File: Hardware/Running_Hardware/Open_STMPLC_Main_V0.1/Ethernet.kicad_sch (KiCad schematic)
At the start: 19 parts, among them J13 RJ45_Hanrun_HR911105A_Horizon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, U7 LAN8720A, Y3 25MHz

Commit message: PCB routing completion v0.1 Main
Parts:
- added C73: 1nF/2kV, Capacitor_SMD:C_1206_3216Metric_Pad1.33x1.80mm_HandSolder, symbol Device:C_Small
- added R17, R48, R49: 10K, Resistor_SMD:R_0603_1608Metric_Pad0.98x0.95mm_HandSolder, symbol Device:R_Small
- added R30: 1M, Resistor_SMD:R_1206_3216Metric_Pad1.30x1.75mm_HandSolder, symbol Device:R_Small
- U7: footprint Package_DFN_QFN:VQFN-24-1EP_4x4mm_P0.5mm_EP2.5x2.5mm_ThermalVias -> Package_DFN_QFN:VQFN-24-1EP_4x4mm_P0.5mm_EP2.5x2.5mm
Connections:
- net +3V3: no longer R27.2, R28.2
- net GND: now also J13.10, J13.11, C73.2, R17.1, R30.1, R48.2; no longer J13.SH
- net LED1: now also R27.2; no longer J13.11
- net LED2: now also R28.2, R17.2; no longer J13.10
- net at C38.1, C39.1, C40.1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: now also R49.1
- net ETH_RXER renamed PHYAD0
- net PHYAD0: now also R48.1, R49.2
- net Earth: no longer names the net of J13.8
- net Earth: now also J13.SH, C73.1, R30.2
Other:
- moved on the sheet: R27, R28

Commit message: Silkscreen and DRC
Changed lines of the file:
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@@
 	(title_block
 		(title "Open_STMPLC_Main")
-		(date "2026-05-23")
+		(date "2026-05-24")
 		(rev "0.1")
 	)
@@
 		(effects
 			(font
-				(size 1.27 1.27)
+				(size 1 1)
 			)
 			(justify left bottom)
@@
 		(effects
 			(font
-				(size 1.27 1.27)
+				(size 1 1)
 			)
 			(justify left bottom)
@@
 		(effects
 			(font
-				(size 1.27 1.27)
+				(size 1 1)
 			)
 			(justify left bottom)
@@
 		(effects
 			(font
-				(size 1.27 1.27)
+				(size 1 1)
 			)
 			(justify left bottom)
@@
 		(effects
 			(font
-				(size 1.27 1.27)
+				(size 1 1)
 			)
 			(justify left bottom)
@@
 			(effects
 				(font
-					(size 1.27 1.27)
+					(size 1 1)
 				)
 			)
@@
 			(effects
 				(font
-					(size 1.27 1.27)
-				)
-			)
+					(size 1 1)
+				)
+			)

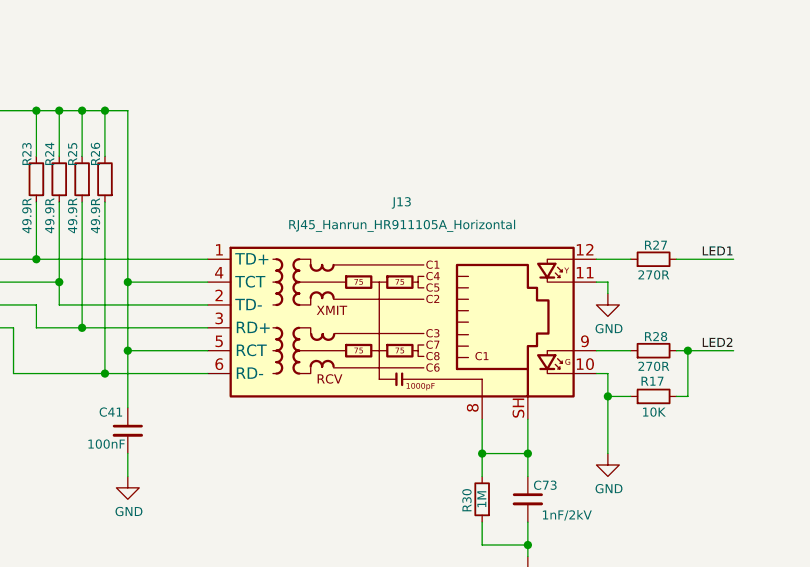
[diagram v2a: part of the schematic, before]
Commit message: Ethernet updated to vertical
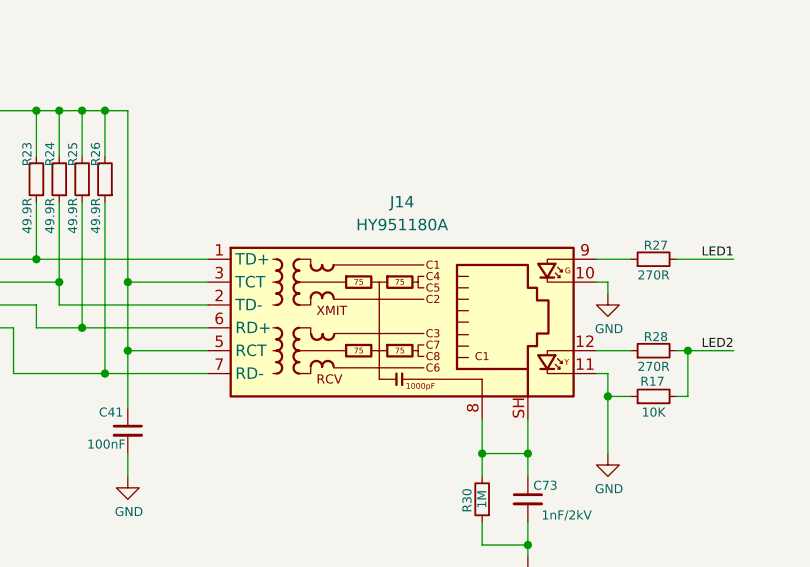
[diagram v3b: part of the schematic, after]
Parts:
- removed J13: RJ45_Hanrun_HR911105A_Horizontal, Connector_RJ:RJ45_Hanrun_HR911105A_Horizontal, symbol Connector:RJ45_Hanrun_HR911105A_Horizontal
- added J14: HY951180A, HY951180A:HY951180A, symbol HY951180A:HY951180A
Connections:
- net GND: now also J14.10, J14.11
- net RD+: now also J14.6 (RD+)
- net RD-: now also J14.7 (RD-)
- net TD+: now also J14.1 (TD+)
- net TD-: now also J14.2 (TD-)
- net at C38.1, C39.1, C40.1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: now also J14.3 (TCT), J14.5 (RCT)
- net at R28.1: now also J14.12
- net at R27.1: now also J14.9
- net at C73.1, R30.2: now also J14.8, J14.SH
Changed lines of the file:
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@@
+	)
+	(symbol
+		(lib_id "HY951180A:HY951180A")
+		(at 200.66 93.98 0)
+		(unit 1)
+		(exclude_from_sim no)
+		(in_bom yes)
+		(on_board yes)
+		(dnp no)
+		(fields_autoplaced yes)
+		(property "Reference" "J14"
+			(at 201.93 80.01 0)
+			(effects
+				(font
+					(size 1.27 1.27)
+				)
+			)
+		)
+		(property "Value" "HY951180A"
+			(at 201.93 82.55 0)
+			(effects
+				(font
+					(size 1.27 1.27)
+				)
+			)
+		)
+		(property "Footprint" "HY951180A:HY951180A"
+			(at 200.66 81.28 0)
+			(effects
+				(font
+					(size 1.27 1.27)
+				)
+				(hide yes)
+			)
+		)
+		(property "Datasheet" ""
+			(at 200.66 78.74 0)
+			(effects
+				(font
+					(size 1.27 1.27)
+				)
+				(hide yes)
+			)
+		)
+		(property "Description" ""
+			(at 200.66 93.98 0)
+			(effects
+				(font
+					(size 1.27 1.27)
+				)
+				(hide yes)
+			)
+		)
+		(pin "3"
+		)
+		(pin "1"
+		)
+		(pin "12"
+		)
+		(pin "4"
+		)
+		(pin "2"
+		)
+		(pin "9"
+		)
+		(pin "7"
+		)
+		(pin "SH"
+		)
+		(pin "8"
+		)
+		(pin "6"
+		)
+		(pin "5"
+		)
+		(pin "10"
+		)
+		(pin "11"
+		)
+		(instances
+			(project "Open_STMPLC_Main_V0.1"
+				(path "/0b17c9ff-697e-478a-b9b2-a0c5b14c9e6c/2c4ca765-43c3-4f95-8835-dba7f06999bb"
+					(reference "J14")
+					(unit 1)
+				)
+			)
+		)
 	)
 	(symbol
@@
 					(unit 1)
 				)
-			)
-		)
-	)
-	(symbol
-		(lib_id "Connector:RJ45_Hanrun_HR911105A_Horizontal")
-		(at 200.66 93.98 0)
-		(unit 1)
-		(exclude_from_sim no)
-		(in_bom yes)
-		(on_board yes)
-		(dnp no)
-		(fields_autoplaced yes)
-		(property "Reference" "J13"
-			(at 201.93 80.01 0)
-			(effects
-				(font
-					(size 1 1)
-				)
-			)
-		)
-		(property "Value" "RJ45_Hanrun_HR911105A_Horizontal"
-			(at 201.93 82.55 0)
-			(effects
-				(font
-					(size 1 1)
-				)
-			)
-		)
-		(property "Footprint" "Connector_RJ:RJ45_Hanrun_HR911105A_Horizontal"
-			(at 200.66 81.28 0)
-			(effects
-				(font
-					(size 1.27 1.27)
-				)
-				(hide yes)
-			)
-		)
-		(property "Datasheet" "https://datasheet.lcsc.com/lcsc/1811141815_HANRUN-Zhongshan-HanRun-Elec-HR911105A_C12074.pdf"
-			(at 200.66 78.74 0)
-			(effects
-				(font
-					(size 1.27 1.27)
-				)
-				(hide yes)
-			)
-		)
-		(property "Description" "1 Port RJ45 Magjack Connector Through Hole 10/100 Base-T, AutoMDIX"
-			(at 200.66 93.98 0)
-			(effects
-				(font
-					(size 1.27 1.27)
-				)
-				(hide yes)
-			)
-		)
-		(pin "12"
-		)
-		(pin "9"
-		)
-		(pin "7"
-		)
-		(pin "3"
-		)
-		(pin "2"
-		)
-		(pin "6"
-		)
-		(pin "SH"
-		)
-		(pin "11"
-		)
-		(pin "5"
-		)
-		(pin "10"
-		)
-		(pin "1"
-		)
-		(pin "8"
-		)
-		(pin "4"
-		)
-		(instances
-			(project "Open_STMPLC_Main_V0.1"
-				(path "/0b17c9ff-697e-478a-b9b2-a0c5b14c9e6c/2c4ca765-43c3-4f95-8835-dba7f06999bb"
-					(reference "J13")
-					(unit 1)
-				)

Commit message: Gerber generation v0.1
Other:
- company: (none) -> Thingslista Automation LLP
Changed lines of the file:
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@@
 	(title_block
 		(title "Open_STMPLC_Main")
-		(date "2026-05-24")
+		(date "2026-06-03")
 		(rev "0.1")
+		(company "Thingslista Automation LLP")
 	)
 	(rectangle
